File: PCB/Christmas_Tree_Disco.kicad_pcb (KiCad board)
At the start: 2 copper layers, 190.5 x 188.9 mm, 121 parts, among them J1 PJ-006B-SMT-TR, U1 DEV_KIT_EK-TM4C123GXL, U2 TLC5955DCA, U3 LM1085-5.0, U301 MC14504B

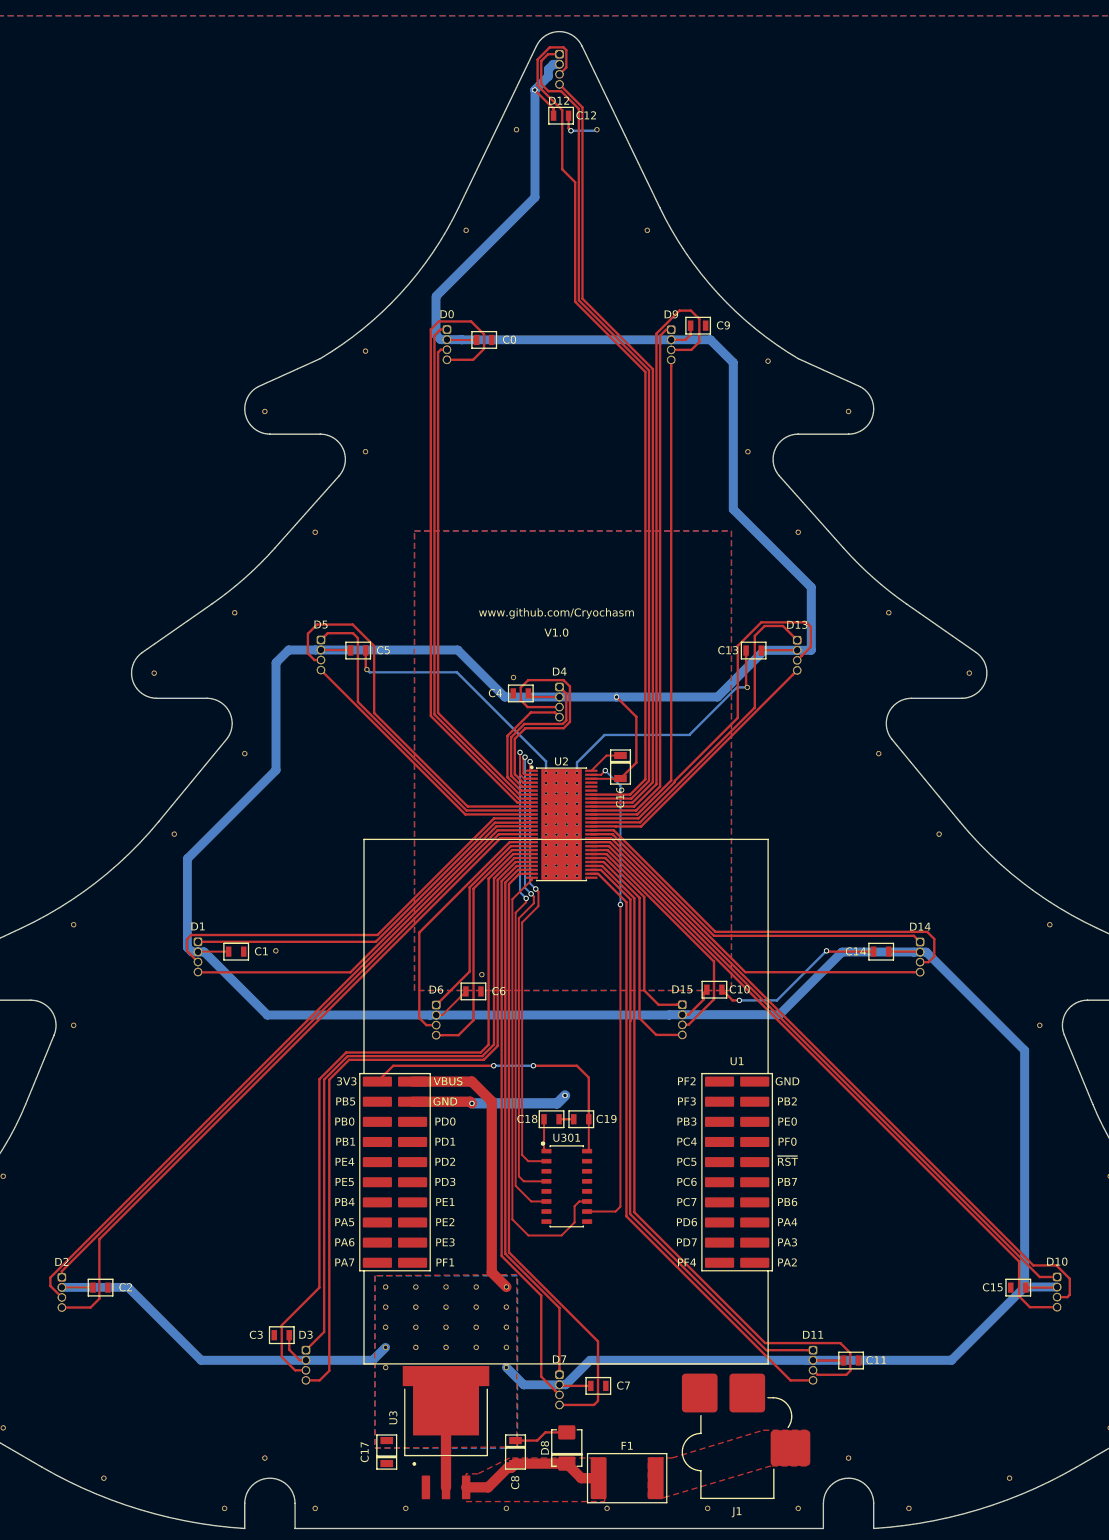
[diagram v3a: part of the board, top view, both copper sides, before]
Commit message: V1.0 Ready for Review
Added compatability with the 430BOOST-C55AUDIO1 booster pack.
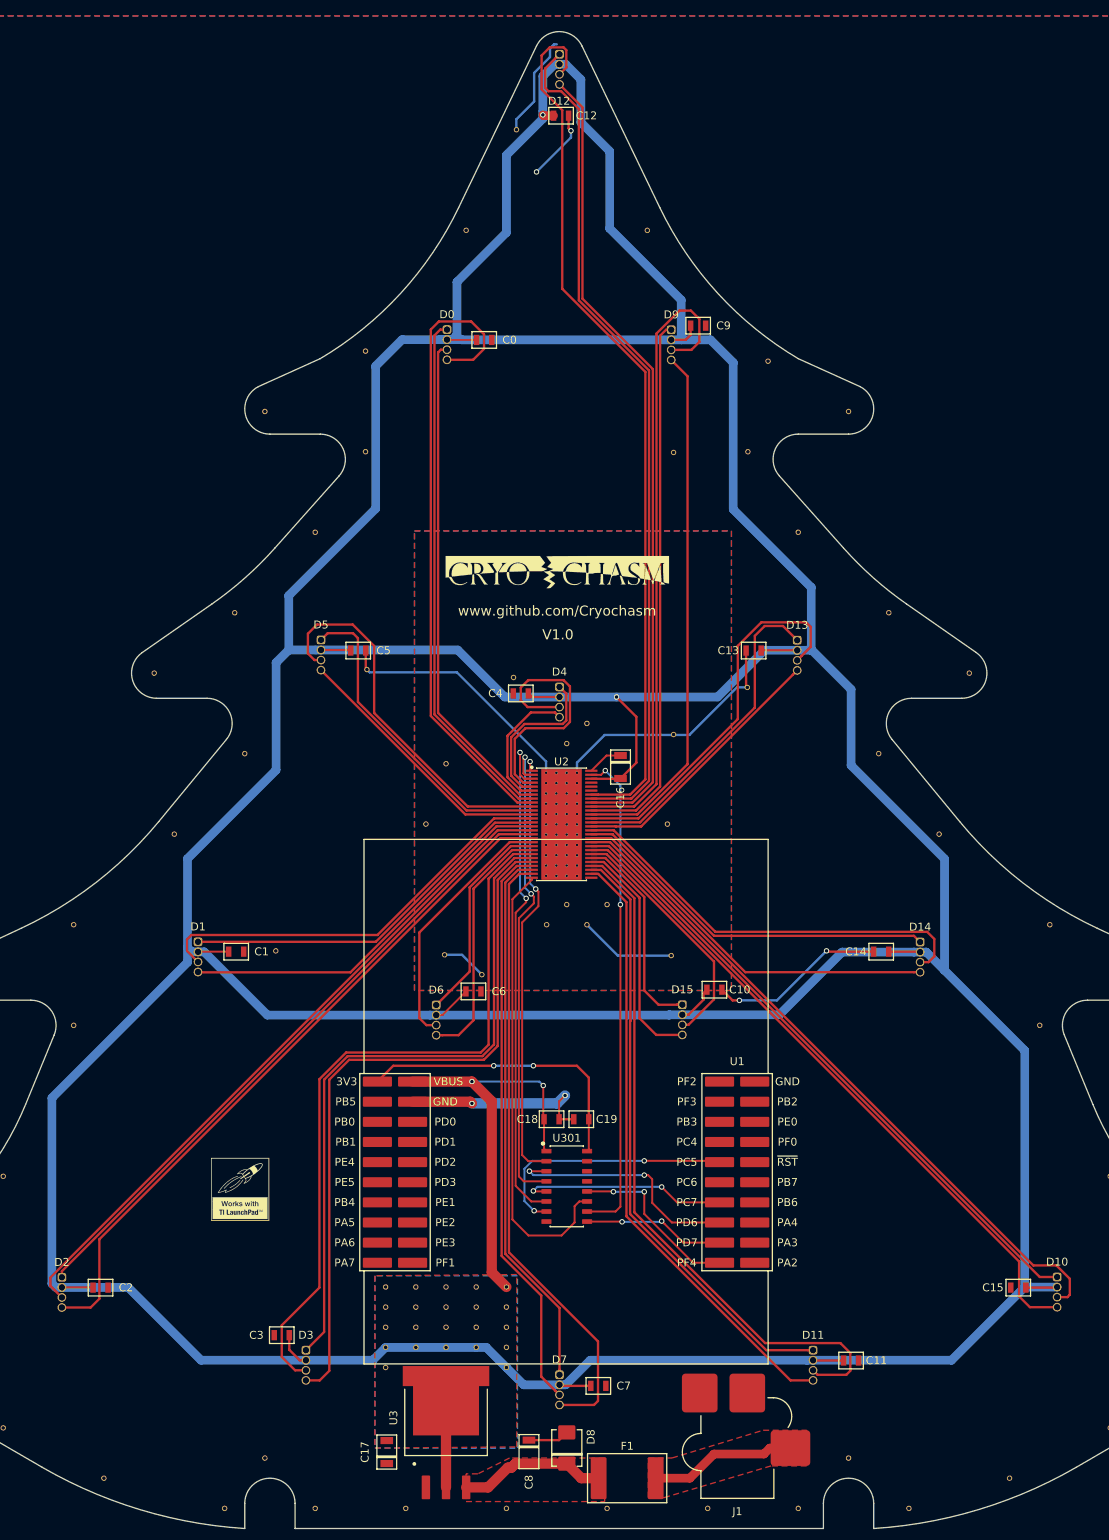
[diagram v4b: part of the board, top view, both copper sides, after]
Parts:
- removed the STITCH at (113.0, 39.4)
- added H1: LPRocket, local:LPRocket, F.Cu at (68.0, 173.1)
- added STITCH: VIA-432-686, local:VIA-432-686, F.Cu at (122.7, 80.1)
- added STITCH: VIA-432-686, local:VIA-432-686, F.Cu at (109.2, 137.2)
- added STITCH: VIA-432-686, local:VIA-432-686, F.Cu at (106.7, 139.7)
- added STITCH: VIA-432-686, local:VIA-432-686, F.Cu at (111.8, 139.7)
- added STITCH: VIA-432-686, local:VIA-432-686, F.Cu at (114.3, 137.2)
- added STITCH: VIA-432-686, local:VIA-432-686, F.Cu at (93.8, 143.5)
- added STITCH: VIA-432-686, local:VIA-432-686, F.Cu at (122.4, 143.6)
- added STITCH: VIA-432-686, local:VIA-432-686, F.Cu at (122.7, 115.7)
- added STITCH: VIA-432-686, local:VIA-432-686, F.Cu at (121.9, 127.0)
- added STITCH: VIA-432-686, local:VIA-432-686, F.Cu at (91.4, 127.0)
- added STITCH: VIA-432-686, local:VIA-432-686, F.Cu at (94.0, 119.4)
- added STITCH: VIA-432-686, local:VIA-432-686, F.Cu at (111.8, 114.3)
- added STITCH: VIA-432-686, local:VIA-432-686, F.Cu at (109.2, 116.8)
- V1.0: footprint local:PCB-LABEL -> local:Cryochasm
- moved V1.0 6.40 mm to (108.0, 95.2)
- moved C8 1.70 mm to (104.4, 206.2)
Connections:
- J1 pad 3: (no net) -> Net-(J1-Pad3)
- U1 pad 10: (no net) -> Net-(U1-Pad10)
- U1 pad 11: (no net) -> Net-(U1-Pad11)
- U1 pad 12: (no net) -> Net-(U1-Pad12)
- U1 pad 13: (no net) -> Net-(U1-Pad13)
- U1 pad 14: (no net) -> Net-(U1-Pad14)
- U1 pad 15: (no net) -> Net-(U1-Pad15)
- U1 pad 16: (no net) -> Net-(U1-Pad16)
- U1 pad 17: (no net) -> Net-(U1-Pad17)
- U1 pad 18: (no net) -> Net-(U1-Pad18)
- U1 pad 2: (no net) -> Net-(U1-Pad2)
- U1 pad 21: (no net) -> Net-(U1-Pad21)
- U1 pad 22: (no net) -> Net-(U1-Pad22)
- U1 pad 23: (no net) -> Net-(U1-Pad23)
- U1 pad 24: (no net) -> Net-(U1-Pad24)
- U1 pad 25: (no net) -> /Top Sheet/Microcontroller/LAT_3V3
- U1 pad 26: (no net) -> Net-(U1-Pad26)
- U1 pad 27: /Top Sheet/Microcontroller/LAT_3V3 -> /Top Sheet/Microcontroller/SCLK_3V3
- U1 pad 28: /Top Sheet/Microcontroller/SCLK_3V3 -> /Top Sheet/Microcontroller/DATA_3V3
- U1 pad 29: /Top Sheet/Microcontroller/DATA_3V3 -> /Top Sheet/Microcontroller/GSCLK_3V3
- U1 pad 3: (no net) -> Net-(U1-Pad3)
- U1 pad 30: /Top Sheet/Microcontroller/GSCLK_3V3 -> /Top Sheet/Microcontroller/ERROR_RD_3V3
- U1 pad 31: /Top Sheet/Microcontroller/ERROR_RD_3V3 -> Net-(U1-Pad31)
- U1 pad 32: (no net) -> Net-(U1-Pad32)
- U1 pad 33: (no net) -> Net-(U1-Pad33)
- U1 pad 34: (no net) -> Net-(U1-Pad34)
- U1 pad 35: (no net) -> Net-(U1-Pad35)
- U1 pad 36: (no net) -> Net-(U1-Pad36)
- U1 pad 37: (no net) -> Net-(U1-Pad37)
- U1 pad 38: (no net) -> Net-(U1-Pad38)
- U1 pad 39: (no net) -> Net-(U1-Pad39)
- U1 pad 4: (no net) -> Net-(U1-Pad4)
- U1 pad 5: (no net) -> Net-(U1-Pad5)
- U1 pad 6: (no net) -> Net-(U1-Pad6)
- U1 pad 7: (no net) -> Net-(U1-Pad7)
- U1 pad 8: (no net) -> Net-(U1-Pad8)
- U1 pad 9: (no net) -> Net-(U1-Pad9)
- U2 pad 51: (no net) -> Net-(U2-Pad51)
- U2 pad 52: (no net) -> Net-(U2-Pad52)
- U2 pad 53: (no net) -> Net-(U2-Pad53)
- U301 pad 14: (no net) -> Net-(U301-Pad14)
- U301 pad 15: (no net) -> Net-(U301-Pad15)
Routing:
- net /Top Sheet/Microcontroller/5V: track 629.8 -> 847.7 mm, vias 2 -> 4
- net /Top Sheet/Microcontroller/GND: track 123.4 -> 159.8 mm, vias 5 -> 6
- net /Top Sheet/Microcontroller/LAT_3V3: track 0.00 -> 32.5 mm, vias 0 -> 2
- net /Top Sheet/Microcontroller/DATA_3V3: track 0.00 -> 30.6 mm, vias 0 -> 2
- net /Top Sheet/Microcontroller/SCLK_3V3: track 0.00 -> 26.2 mm, vias 0 -> 2
- net /Top Sheet/Microcontroller/ERROR_RD_3V3: track 0.00 -> 22.1 mm, vias 0 -> 2
- net /Top Sheet/Power Supply/VIN: track 0.00 -> 18.6 mm
- net /Top Sheet/Microcontroller/GSCLK_3V3: track 0.00 -> 17.9 mm, vias 0 -> 2
- net /Top Sheet/RGB LED Array/RGB09_2: track 64.9 -> 66.6 mm
- net /Top Sheet/RGB LED Array/RGB12_1: track 108.3 -> 107.0 mm

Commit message: Gerber Updates
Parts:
- added H5: Power Supply 12V 24W, local:Do_Not_Populate, F.Cu at (229.4, 187.8)
- added H6: Power Info, local:Polarity, F.Cu at (155.8, 208.8)
- renumbered H301 to H2, H302 to H4, U301 to U4
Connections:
- J1 pad 3: Net-(J1-Pad3) -> (no net)
- U1 pad 10: Net-(U1-Pad10) -> (no net)
- U1 pad 11: Net-(U1-Pad11) -> (no net)
- U1 pad 12: Net-(U1-Pad12) -> (no net)
- U1 pad 13: Net-(U1-Pad13) -> (no net)
- U1 pad 14: Net-(U1-Pad14) -> (no net)
- U1 pad 15: Net-(U1-Pad15) -> (no net)
- U1 pad 16: Net-(U1-Pad16) -> (no net)
- U1 pad 17: Net-(U1-Pad17) -> (no net)
- U1 pad 18: Net-(U1-Pad18) -> (no net)
- U1 pad 2: Net-(U1-Pad2) -> (no net)
- U1 pad 21: Net-(U1-Pad21) -> (no net)
- U1 pad 22: Net-(U1-Pad22) -> (no net)
- U1 pad 23: Net-(U1-Pad23) -> (no net)
- U1 pad 24: Net-(U1-Pad24) -> (no net)
- U1 pad 26: Net-(U1-Pad26) -> (no net)
- U1 pad 3: Net-(U1-Pad3) -> (no net)
- U1 pad 31: Net-(U1-Pad31) -> (no net)
- U1 pad 32: Net-(U1-Pad32) -> (no net)
- U1 pad 33: Net-(U1-Pad33) -> (no net)
- U1 pad 34: Net-(U1-Pad34) -> (no net)
- U1 pad 35: Net-(U1-Pad35) -> (no net)
- U1 pad 36: Net-(U1-Pad36) -> (no net)
- U1 pad 37: Net-(U1-Pad37) -> (no net)
- U1 pad 38: Net-(U1-Pad38) -> (no net)
- U1 pad 39: Net-(U1-Pad39) -> (no net)
- U1 pad 4: Net-(U1-Pad4) -> (no net)
- U1 pad 5: Net-(U1-Pad5) -> (no net)
- U1 pad 6: Net-(U1-Pad6) -> (no net)
- U1 pad 7: Net-(U1-Pad7) -> (no net)
- U1 pad 8: Net-(U1-Pad8) -> (no net)
- U1 pad 9: Net-(U1-Pad9) -> (no net)
- U2 pad 51: Net-(U2-Pad51) -> (no net)
- U2 pad 52: Net-(U2-Pad52) -> (no net)
- U2 pad 53: Net-(U2-Pad53) -> (no net)
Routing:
- net /Top Sheet/Power Supply/VIN_FUSED: track 18.7 -> 2.18 mm
- net /Top Sheet/Microcontroller/GND: track 159.8 -> 168.2 mm

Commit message: Added Open Hardware Logo
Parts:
- added H7: SPFMDBC, local:Open_Source_HW_Logo, F.Cu at (149.4, 173.2)
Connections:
- J1 pad 3: (no net) -> Net-(J1-Pad3)
- U1 pad 10: (no net) -> Net-(U1-Pad10)
- U1 pad 11: (no net) -> Net-(U1-Pad11)
- U1 pad 12: (no net) -> Net-(U1-Pad12)
- U1 pad 13: (no net) -> Net-(U1-Pad13)
- U1 pad 14: (no net) -> Net-(U1-Pad14)
- U1 pad 15: (no net) -> Net-(U1-Pad15)
- U1 pad 16: (no net) -> Net-(U1-Pad16)
- U1 pad 17: (no net) -> Net-(U1-Pad17)
- U1 pad 18: (no net) -> Net-(U1-Pad18)
- U1 pad 2: (no net) -> Net-(U1-Pad2)
- U1 pad 21: (no net) -> Net-(U1-Pad21)
- U1 pad 22: (no net) -> Net-(U1-Pad22)
- U1 pad 23: (no net) -> Net-(U1-Pad23)
- U1 pad 24: (no net) -> Net-(U1-Pad24)
- U1 pad 26: (no net) -> Net-(U1-Pad26)
- U1 pad 3: (no net) -> Net-(U1-Pad3)
- U1 pad 31: (no net) -> Net-(U1-Pad31)
- U1 pad 32: (no net) -> Net-(U1-Pad32)
- U1 pad 33: (no net) -> Net-(U1-Pad33)
- U1 pad 34: (no net) -> Net-(U1-Pad34)
- U1 pad 35: (no net) -> Net-(U1-Pad35)
- U1 pad 36: (no net) -> Net-(U1-Pad36)
- U1 pad 37: (no net) -> Net-(U1-Pad37)
- U1 pad 38: (no net) -> Net-(U1-Pad38)
- U1 pad 39: (no net) -> Net-(U1-Pad39)
- U1 pad 4: (no net) -> Net-(U1-Pad4)
- U1 pad 5: (no net) -> Net-(U1-Pad5)
- U1 pad 6: (no net) -> Net-(U1-Pad6)
- U1 pad 7: (no net) -> Net-(U1-Pad7)
- U1 pad 8: (no net) -> Net-(U1-Pad8)
- U1 pad 9: (no net) -> Net-(U1-Pad9)
- U2 pad 51: (no net) -> Net-(U2-Pad51)
- U2 pad 52: (no net) -> Net-(U2-Pad52)
- U2 pad 53: (no net) -> Net-(U2-Pad53)
- U4 pad 14: Net-(U4-Pad14) -> (no net)
- U4 pad 15: Net-(U4-Pad15) -> (no net)
